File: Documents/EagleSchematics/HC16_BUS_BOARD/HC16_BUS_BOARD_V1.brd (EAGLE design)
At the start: 113 x 97.5 mm, 19 parts, among them Q1 TIP120, Q2 TIP120, Q3 TIP120, Q4 TIP120

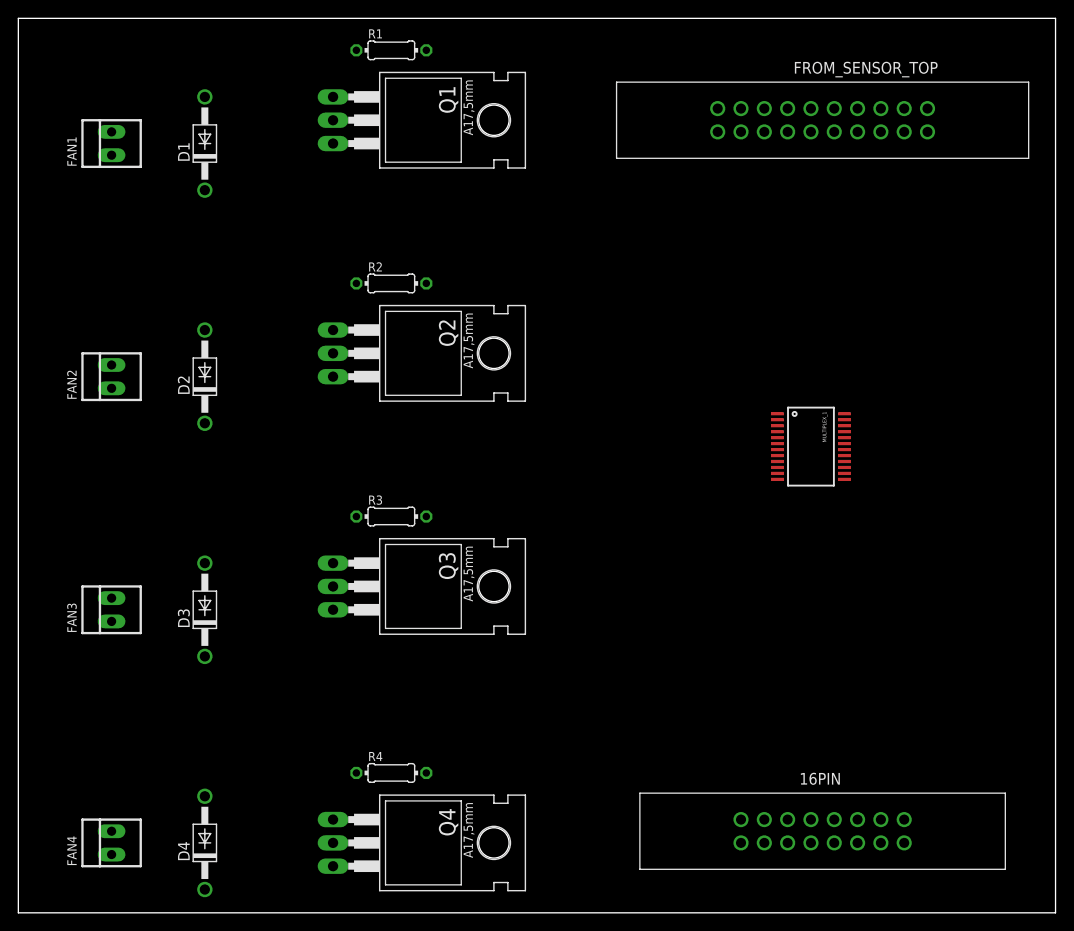
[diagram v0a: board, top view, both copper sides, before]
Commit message: Eagle Schematics
Changed array of sensornetwork
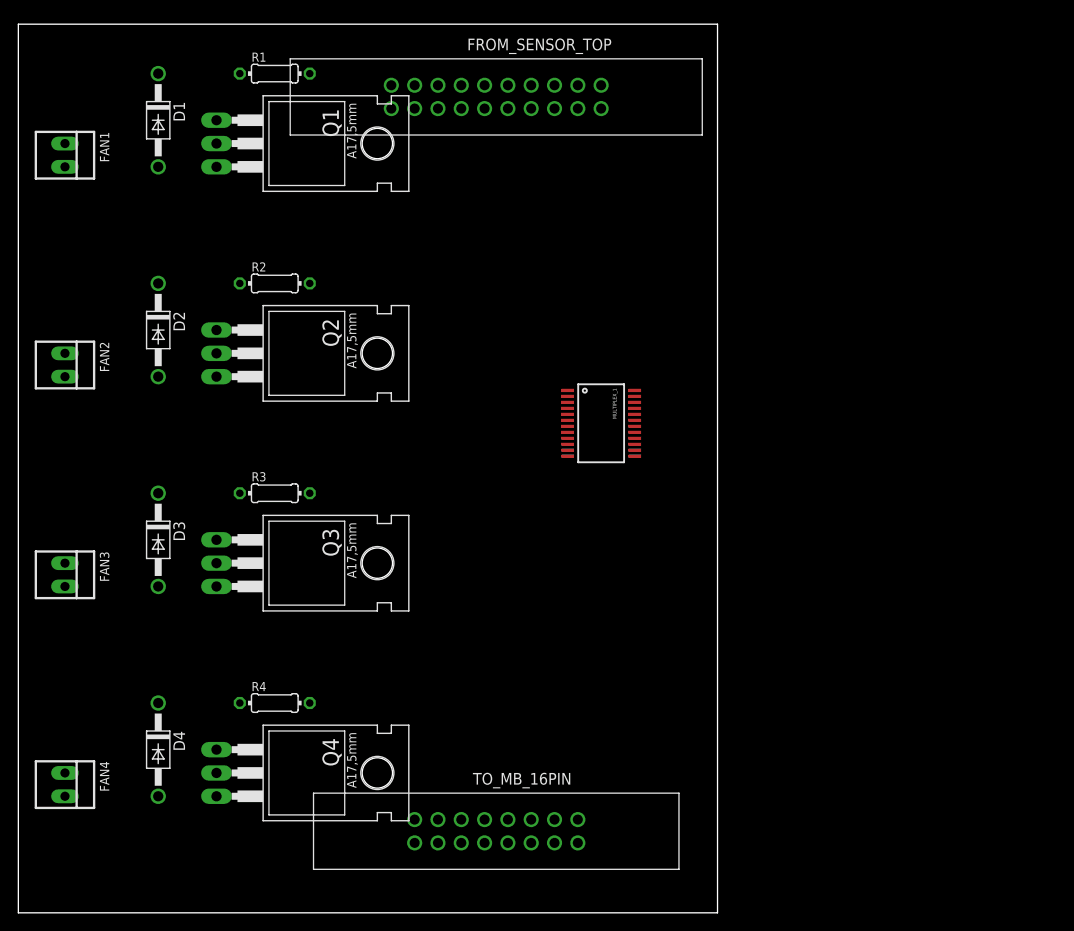
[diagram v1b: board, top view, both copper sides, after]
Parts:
- removed 16PIN: 61201622021, Wuerth_Elektronik_eiCan_05_Box_Header_IDC_Connectors_1_2:61201622021
- added TO_MB_16PIN: 61201622021, Wuerth_Elektronik_eiCan_05_Box_Header_IDC_Connectors_1_2:61201622021
- moved FROM_SENSOR_TOP 35.7 mm to (58.4, 88.9)
- moved MULTIPLEX_1 23.0 mm to (63.5, 53.3)
- moved Q4 14.8 mm to (27.9, 15.2)
- moved R4 14.8 mm to (27.9, 22.9)
- moved Q1 13.0 mm to (27.9, 83.8)
- moved Q3 13.0 mm to (27.9, 38.1)
- moved R1 13.0 mm to (27.9, 91.4)
- moved R3 13.0 mm to (27.9, 45.7)
- moved Q2 12.7 mm to (27.9, 61.0)
- moved R2 12.7 mm to (27.9, 68.6)
- moved D4 11.4 mm to (15.2, 17.8), turned to 270 degrees
- moved D3 9.16 mm to (15.2, 40.6), turned to 270 degrees
- moved FAN4 8.13 mm to (5.08, 14.0), turned to 270 degrees
- moved D2 7.18 mm to (15.2, 63.5), turned to 270 degrees
- moved FAN3 6.35 mm to (5.08, 36.8), turned to 270 degrees
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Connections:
- net +12V: now also TO_MB_16PIN.13; no longer 16PIN.13
- net +3V3: now also TO_MB_16PIN.11; no longer 16PIN.11
- net DIG1: now also TO_MB_16PIN.2; no longer 16PIN.2
- net DIG2: now also TO_MB_16PIN.4; no longer 16PIN.4
- net DIG3: now also TO_MB_16PIN.6; no longer 16PIN.6
- net DIG4: now also TO_MB_16PIN.8; no longer 16PIN.8
- net GND: now also TO_MB_16PIN.15; no longer 16PIN.15
- net MUX1: now also TO_MB_16PIN.16; no longer 16PIN.16
- net PWM_FAN1: now also TO_MB_16PIN.1; no longer 16PIN.1
- net PWM_FAN2: now also TO_MB_16PIN.3; no longer 16PIN.3
- net PWM_FAN3: now also TO_MB_16PIN.5; no longer 16PIN.5
- net PWM_FAN4: now also TO_MB_16PIN.7; no longer 16PIN.7
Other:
- board size 113 x 97.5 mm -> 76.2 x 96.8 mm
